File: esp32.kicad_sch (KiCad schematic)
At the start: 22 parts, among them SW1 SW_Push, SW2 SW_Push, U5 ESP32-WROOM-32D

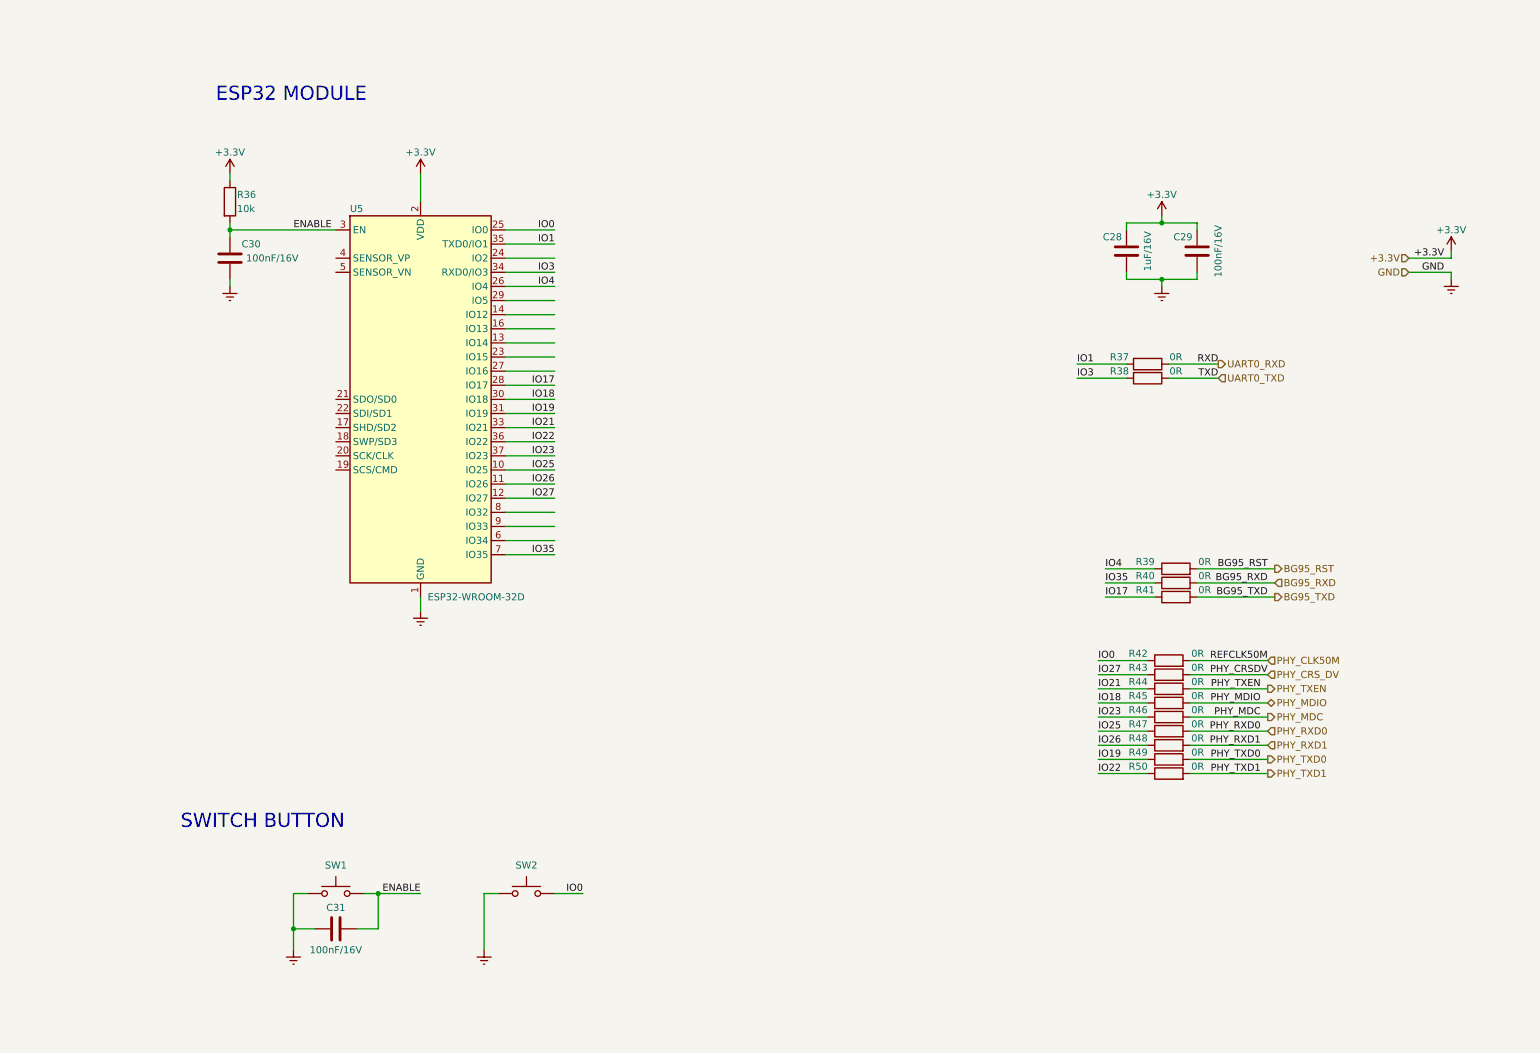
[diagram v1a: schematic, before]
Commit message: Inserido encapsulamento 0603 para os resistores
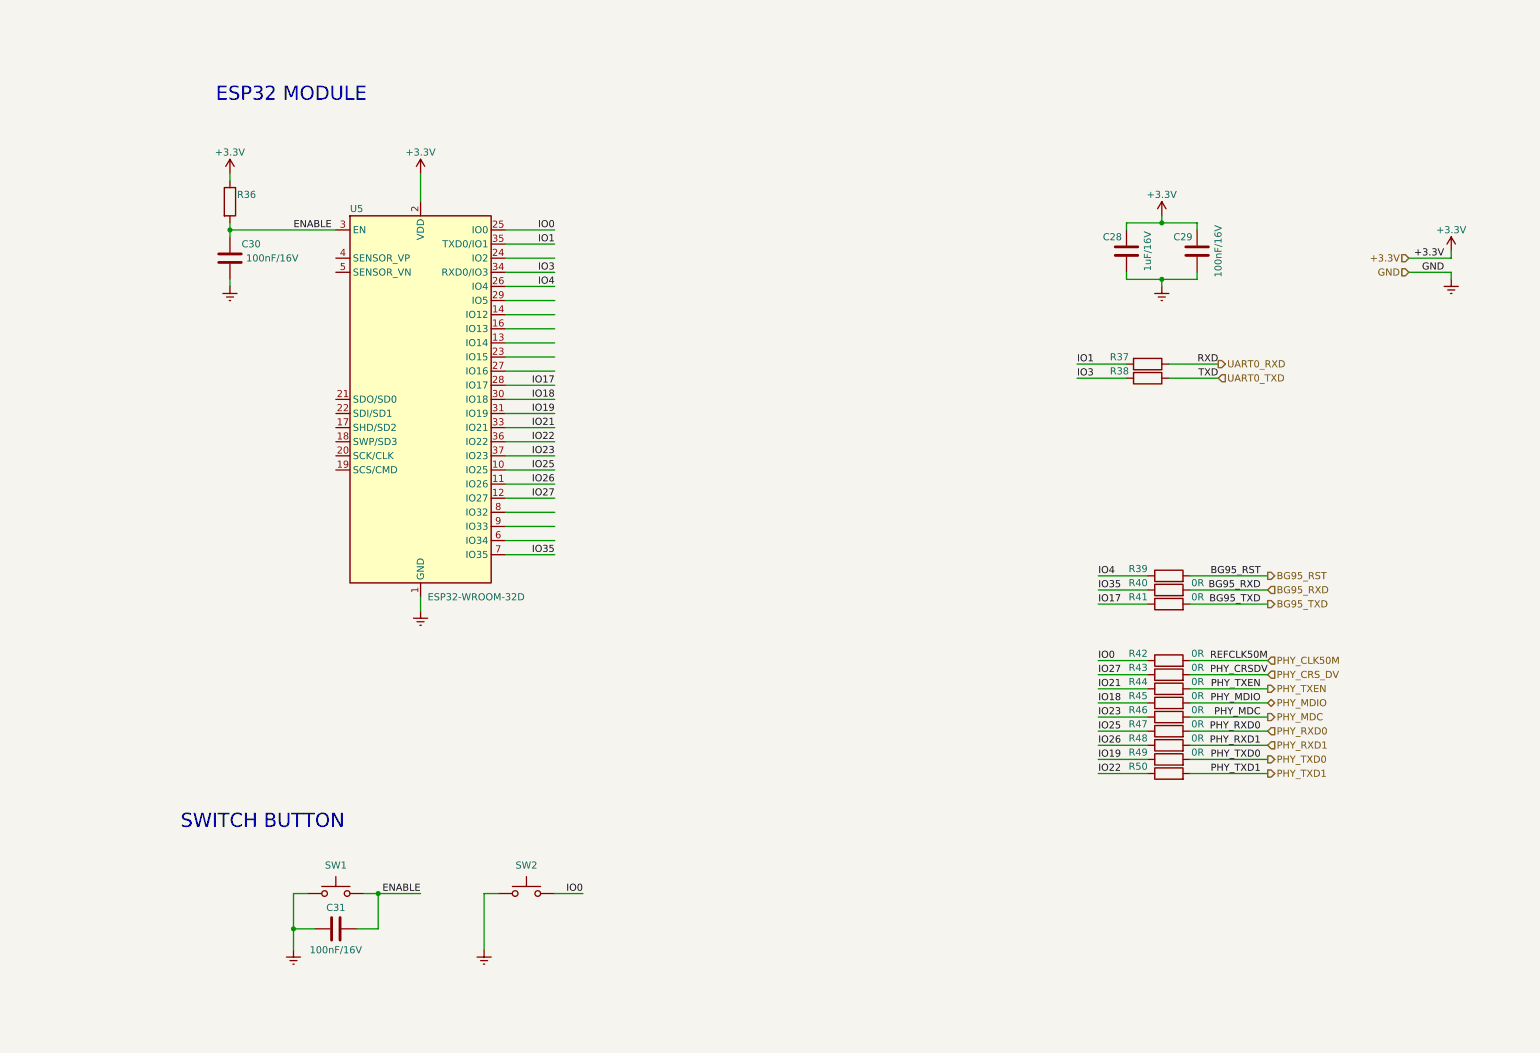
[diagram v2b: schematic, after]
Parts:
- R36: value 10k -> (none)
- R37, R38, R39, R50: value 0R -> (none); footprint Resistor_SMD:R_0402_1005Metric_Pad0.72x0.64mm_HandSolder -> (none)
- R40, R41, R42, R43, R44, R45, R46, R47, R48, R49: footprint Resistor_SMD:R_0402_1005Metric_Pad0.72x0.64mm_HandSolder -> Resistor_SMD:R_0603_1608Metric_Pad0.98x0.95mm_HandSolder
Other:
- moved on the sheet: R39

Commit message: Corrigido alguns ERC e adicionado circuito DTR e RI do BG95
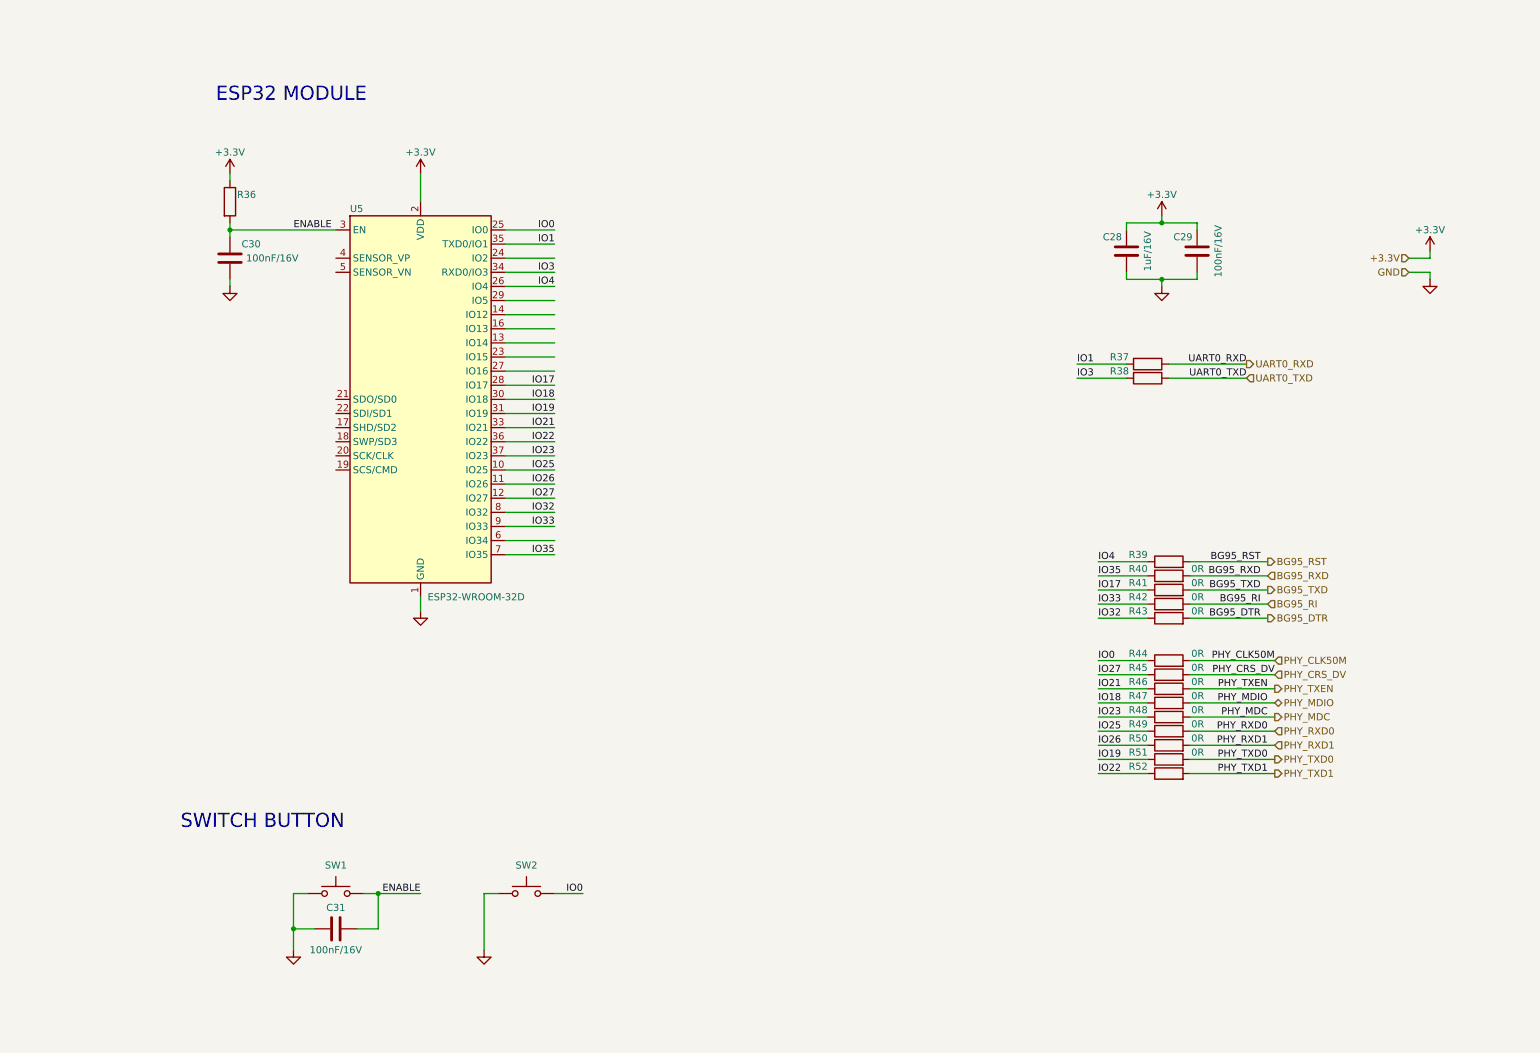
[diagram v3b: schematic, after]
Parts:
- added R42, R43: 0R, Resistor_SMD:R_0603_1608Metric_Pad0.98x0.95mm_HandSolder, symbol Device:R
- renumbered R42 to R44, R43 to R45, R44 to R46, R45 to R47, R46 to R48, R47 to R49, R48 to R50, R49 to R51, R50 to R52
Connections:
- net IO32: now reaches U5.8 (IO32)
- net IO32: now also R43.1
- net IO33: now reaches U5.9 (IO33)
- net IO33: now also R42.1
- net GNDREF renamed GND
- new net BG95_DTR: R43.2
- new net BG95_RI: R42.2
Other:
- moved on the sheet: R39, R40, R41

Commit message: Corrigido todos os ERC
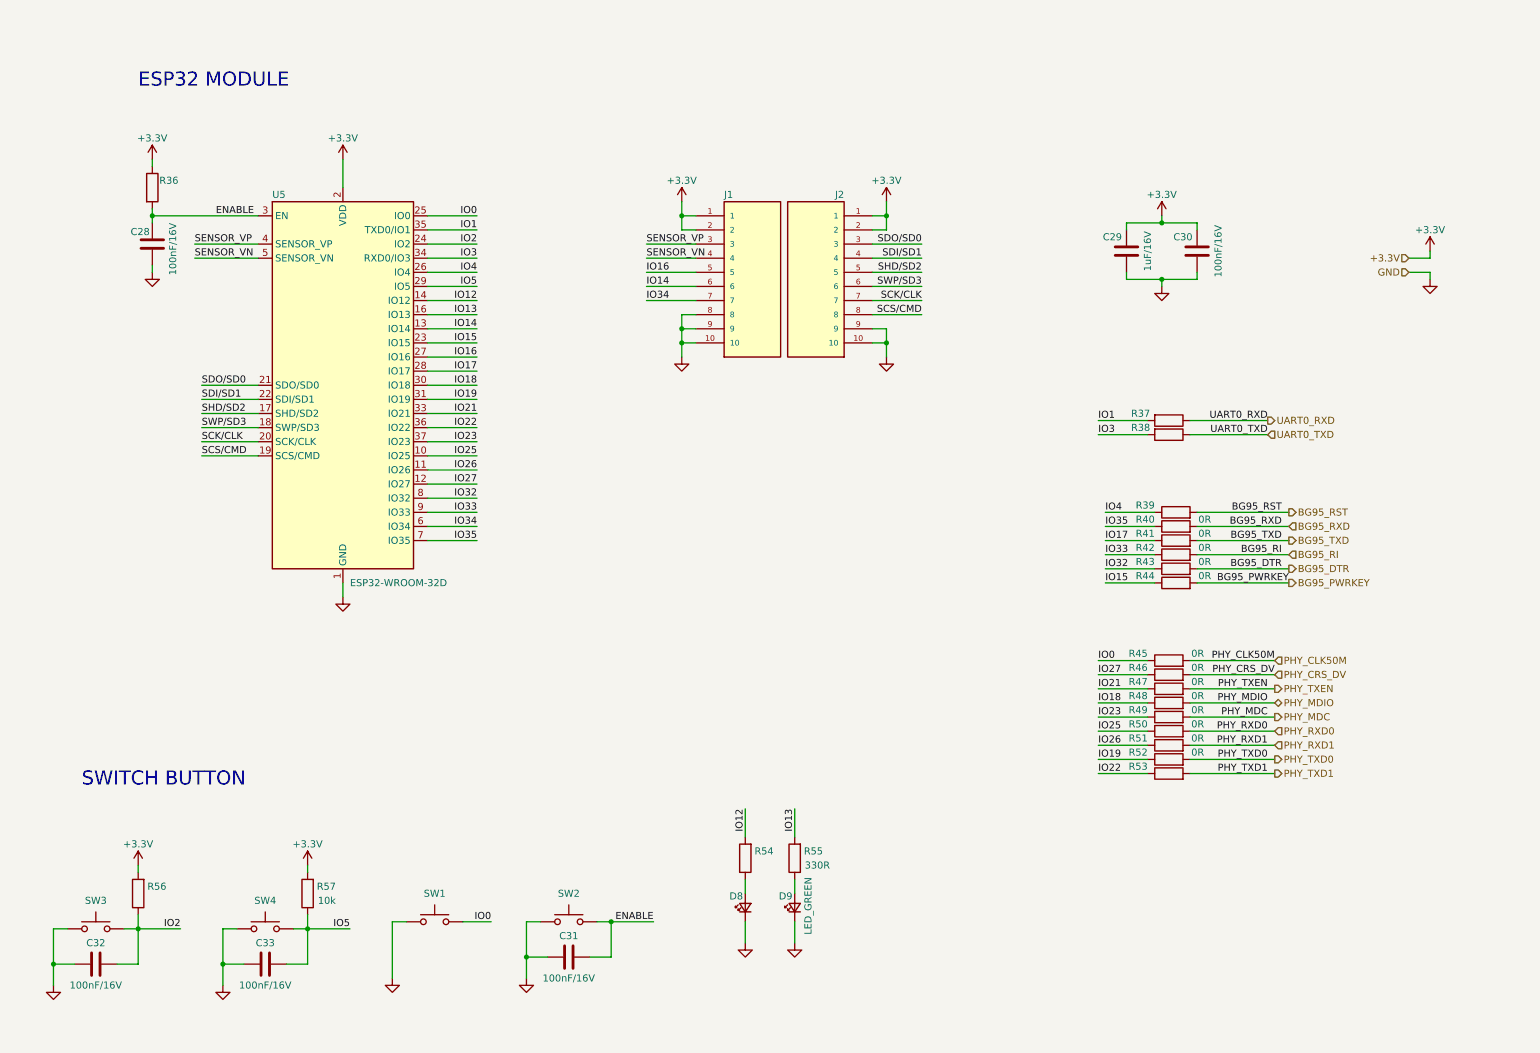
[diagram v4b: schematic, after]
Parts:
- added C31, C33: 100nF/16V, Capacitor_SMD:C_0402_1005Metric_Pad0.74x0.62mm_HandSolder, symbol Device:C
- added D8: (no value), LED_SMD:LED_0603_1608Metric_Pad1.05x0.95mm_HandSolder, symbol Device:LED_Small
- added D9: LED_GREEN, LED_SMD:LED_0603_1608Metric_Pad1.05x0.95mm_HandSolder, symbol Device:LED_Small
- added J1: (no value), symbol Alexandre_Library:104426-8
- added J2: 104426-8, Alexandre_Library:TE_104426-8, symbol Alexandre_Library:104426-8
- added R44: 0R, Resistor_SMD:R_0603_1608Metric_Pad0.98x0.95mm_HandSolder, symbol Device:R
- added R54: (no value), Resistor_SMD:R_0603_1608Metric_Pad0.98x0.95mm_HandSolder, symbol Device:R
- added R55: 330R, Resistor_SMD:R_0603_1608Metric_Pad0.98x0.95mm_HandSolder, symbol Device:R
- added R56: (no value), symbol Device:R
- added R57: 10k, Resistor_SMD:R_0603_1608Metric_Pad0.98x0.95mm_HandSolder, symbol Device:R
- added SW2, SW4: SW_Push, Button_Switch_SMD:SW_SPST_CK_RS282G05A3, symbol Switch:SW_Push
- renumbered C30 to C28, C28 to C29, C29 to C30, C31 to C32, R44 to R45, R45 to R46, R46 to R47, R47 to R48, R48 to R49, R49 to R50, R50 to R51, R51 to R52, R52 to R53, SW2 to SW1, SW1 to SW3
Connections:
- net +3V3: now also J1.1, J1.2, J2.1, J2.2, R56.2, R57.2
- net ENABLE: now also C31.1, SW2.2; no longer C32.1, SW3.2
- net GND: now also C31.2, C33.2, D8.1 (K), D9.1 (K), J1.10, J1.8, J1.9, J2.10, J2.9, SW2.1, SW4.1
- net IO14: now reaches U5.13 (IO14)
- net IO14: now also J1.6
- net IO12: now reaches U5.14 (IO12)
- net IO12: now also R54.2
- net IO13: now reaches U5.16 (IO13)
- net IO13: now also R55.2
- net SHD/SD2: now reaches U5.17 (SHD/SD2)
- net SHD/SD2: now also J2.5
- net SWP/SD3: now reaches U5.18 (SWP/SD3)
- net SWP/SD3: now also J2.6
- net SCS/CMD: now reaches U5.19 (SCS/CMD)
- net SCS/CMD: now also J2.8
- net SCK/CLK: now reaches U5.20 (SCK/CLK)
- net SCK/CLK: now also J2.7
- net SDO/SD0: now reaches U5.21 (SDO/SD0)
- net SDO/SD0: now also J2.3
- net SDI/SD1: now reaches U5.22 (SDI/SD1)
- net SDI/SD1: now also J2.4
- net IO15: now reaches U5.23 (IO15)
- net IO15: now also R44.1
- net IO2: now reaches U5.24 (IO2)
- net IO2: now also C32.1, SW3.2, R56.1
- net IO16: now reaches U5.27 (IO16)
- net IO16: now also J1.5
- net IO5: now reaches U5.29 (IO5)
- net IO5: now also C33.1, R57.1, SW4.2
- net SENSOR_VP: now reaches U5.4 (SENSOR_VP)
- net SENSOR_VP: now also J1.3
- net SENSOR_VN: now reaches U5.5 (SENSOR_VN)
- net SENSOR_VN: now also J1.4
- net IO34: now reaches U5.6 (IO34)
- net IO34: now also J1.7
- new net: D9.2 (A), R55.1
- new net: D8.2 (A), R54.1
- new net BG95_PWRKEY: R44.2
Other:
- moved on the sheet: C28, C32, R36, R37, R38, R39, R40, R41, R42, R43, SW1, SW3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

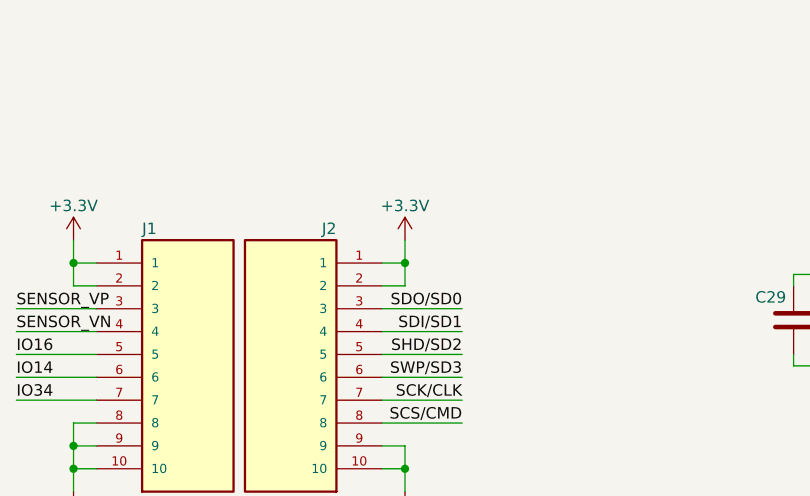
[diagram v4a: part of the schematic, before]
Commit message: Adicionado duas barras de pinos 1x10
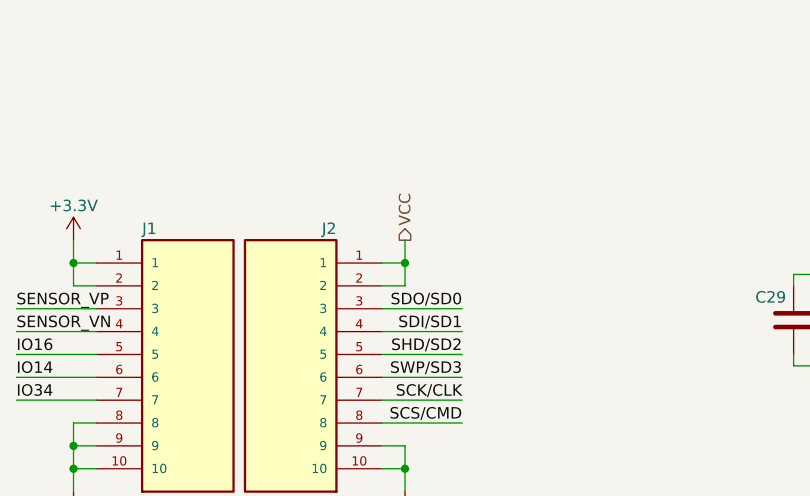
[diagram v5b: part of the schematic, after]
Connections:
- net +3V3: no longer J2.1, J2.2
- new net VCC: J2.1, J2.2
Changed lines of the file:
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@@
     (effects (font (size 1.27 1.27)) (justify right))
+  )
+  (hierarchical_label "VCC" (shape output) (at 168.91 46.99 90)
+    (effects (font (size 1.27 1.27)) (justify left))
   )
   (hierarchical_label "BG95_DTR" (shape output) (at 241.3 113.03 0)
@@
       (effects (font (size 1.27 1.27)) hide)
     )
-    (pin "1")
-  )
-  (symbol (lib_id "power:+3.3V") (at 168.91 46.99 0) (mirror y) (unit 1)
-    (in_bom yes) (on_board yes)
-    (property "Reference" "#PWR070" (id 0) (at 168.91 50.8 0)
-      (effects (font (size 1.27 1.27)) hide)
-    )
-    (property "Value" "+3.3V" (id 1) (at 168.91 43.18 0))
-    (property "Footprint" "" (id 2) (at 168.91 46.99 0)
-      (effects (font (size 1.27 1.27)) hide)
-    )
-    (property "Datasheet" "" (id 3) (at 168.91 46.99 0)
-      (effects (font (size 1.27 1.27)) hide)
-    )

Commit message: Organização do sheet esp32
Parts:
- D8: value (none) -> LED_GREEN
- J1: value (none) -> 104426-8; footprint (none) -> Alexandre_Library:TE_104426-8
- R36, R56: value (none) -> 10k; footprint (none) -> Resistor_SMD:R_0603_1608Metric_Pad0.98x0.95mm_HandSolder
- R37, R38, R39, R53: value (none) -> 0R; footprint (none) -> Resistor_SMD:R_0603_1608Metric_Pad0.98x0.95mm_HandSolder
- R54: value (none) -> 330R
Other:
- note added: "EXTERNAL CONNECTIONS"
- note added: "HEADERS"
- note added: "LEDS"
- note added: "POWER"
- moved on the sheet: C28, C29, C30, C31, C32, C33, D8, D9, J1, J2, R36, R37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
